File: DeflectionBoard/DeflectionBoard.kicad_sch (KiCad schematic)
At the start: 0 parts

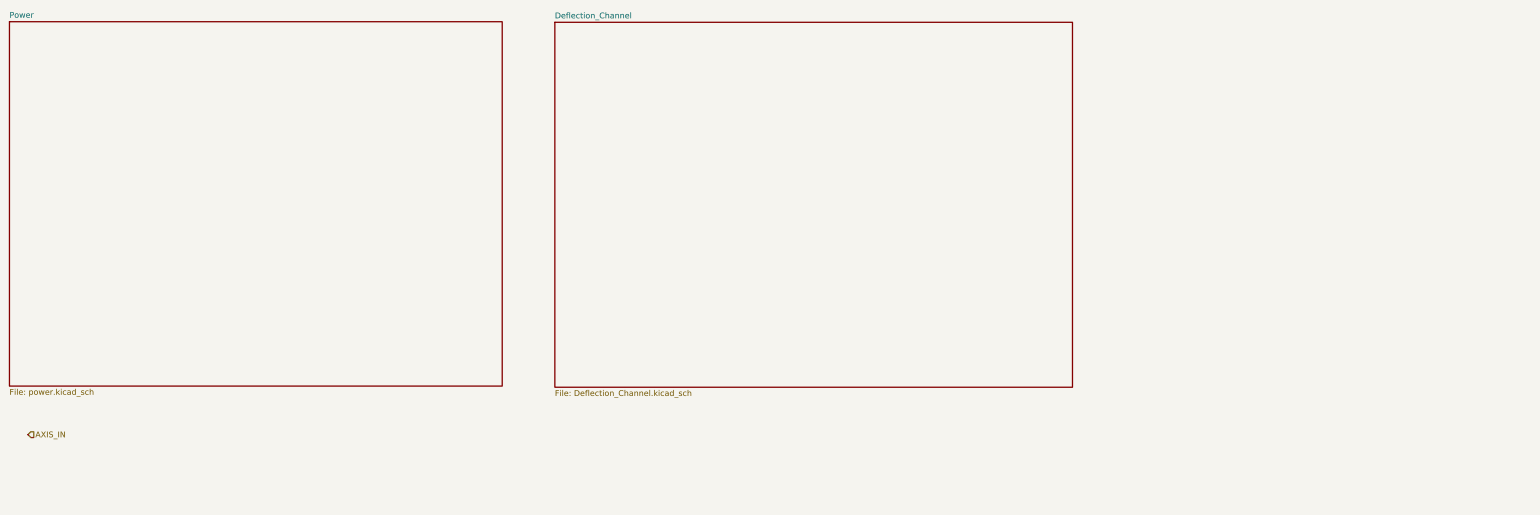
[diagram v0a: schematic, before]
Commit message: DeflectionBoard: channel X + power schematic complete, ERC clean
Full-bridge hysteretic current-mode deflection channel (CSD97394Q4M),
INA240 current sense, OPA2196 input scale, TLV3501 comparator, EN pull-up.
Power: TPS55340 boost (R106=78.7k/~600kHz), AP63205 buck 5V, REF3325 Vmid.
Hierarchical: root + Power + Deflection_Channel sheets, AXIS_IN sheet pin
wired to input connector. 0 ERC violations.

Co-Authored-By: Claude Opus 4.8 <noreply@anthropic.com>
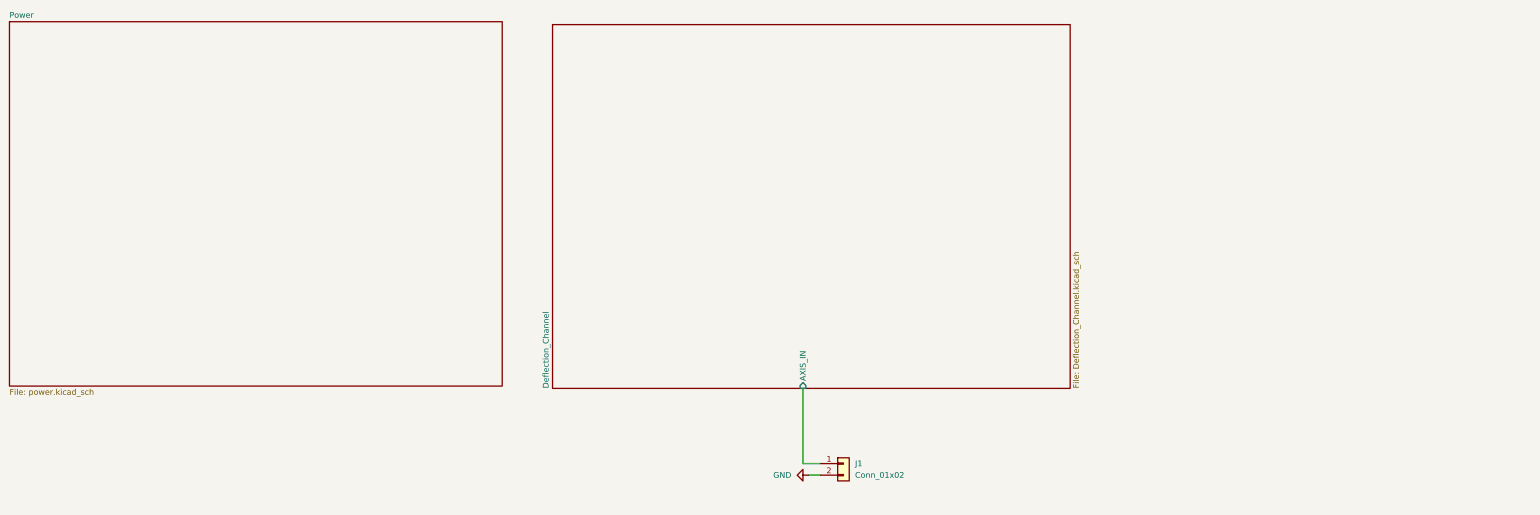
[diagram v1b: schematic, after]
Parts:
- added J1: Conn_01x02, symbol Connector_Generic:Conn_01x02
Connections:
- new net Deflection_Channel/AXIS_IN: J1.1 (Pin_1)
- new net GND: J1.2 (Pin_2)
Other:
- sheet Deflection_Channel ports: added AXIS_IN; removed none
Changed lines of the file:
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@@
 	(generator_version "10.0")
 	(paper "A3")
-	(hierarchical_label "AXIS_IN"
-		(shape input)
-		(at 30.48 115.57 0)
-		(effects
-			(font
-				(size 1.27 1.27)
-			)
-			(justify left)
+	(wire
+		(pts
+			(xy 200.66 105.41) (xy 200.66 121.92)
+		)
+		(stroke
+			(width 0)
+			(type default)
+		)
+	)
+	(wire
+		(pts
+			(xy 200.66 121.92) (xy 204.47 121.92)
+		)
+		(stroke
+			(width 0)
+			(type default)
+		)
+	)
+	(wire
+		(pts
+			(xy 201.93 124.46) (xy 204.47 124.46)
+		)
+		(stroke
+			(width 0)
+			(type default)
+		)
+	)
+	(symbol
+		(lib_id "Connector_Generic:Conn_01x02")
+		(at 209.55 121.92 0)
+		(unit 1)
+		(body_style 1)
+		(exclude_from_sim no)
+		(in_bom yes)
+		(on_board yes)
+		(in_pos_files yes)
+		(dnp no)
+		(fields_autoplaced yes)
+		(property "Reference" "J1"
+			(at 212.09 121.9199 0)
+			(show_name no)
+			(do_not_autoplace no)
+			(effects
+				(font
+					(size 1.27 1.27)
+				)
+				(justify left)
+			)
+		)
+		(property "Value" "Conn_01x02"
+			(at 212.09 124.4599 0)
+			(show_name no)
+			(do_not_autoplace no)
+			(effects
+				(font
+					(size 1.27 1.27)
+				)
+				(justify left)
+			)
+		)
+		(property "Footprint" ""
+			(at 209.55 121.92 0)
+			(hide yes)
+			(show_name no)
+			(do_not_autoplace no)
+			(effects
+				(font
+					(size 1.27 1.27)
+				)
+			)
+		)
+		(property "Datasheet" ""
+			(at 209.55 121.92 0)
+			(hide yes)
+			(show_name no)
+			(do_not_autoplace no)
+			(effects
+				(font
+					(size 1.27 1.27)
+				)
+			)
+		)
+		(property "Description" "Generic connector, single row, 01x02, script generated (kicad-library-utils/schlib/autogen/connector/)"
+			(at 209.55 121.92 0)
+			(hide yes)
+			(show_name no)
+			(do_not_autoplace no)
+			(effects
+				(font
+					(size 1.27 1.27)
+				)
+			)
+		)
+		(pin "1"
+		)
+		(pin "2"
+		)
+		(instances
+			(project "DeflectionBoard"
+				(path "/6f717d52-0a9b-43ca-aa24-dc6f278930de"
+					(reference "J1")
+					(unit 1)
+				)
+			)
+		)
+	)
+	(symbol
+		(lib_id "power:GND")
+		(at 201.93 124.46 270)
+		(unit 1)
+		(body_style 1)
+		(exclude_from_sim no)
+		(in_bom yes)
+		(on_board yes)
+		(in_pos_files yes)
+		(dnp no)
+		(fields_autoplaced yes)
+		(property "Reference" "#PWR01"
+			(at 195.58 124.46 0)
+			(hide yes)
+			(show_name no)
+			(do_not_autoplace no)
+			(effects
+				(font
+					(size 1.27 1.27)
+				)
+			)
+		)
+		(property "Value" "GND"
+			(at 198.12 124.4599 90)
+			(show_name no)
+			(do_not_autoplace no)
+			(effects
+				(font
+					(size 1.27 1.27)
+				)
+				(justify right)
+			)
+		)
+		(property "Footprint" ""
+			(at 201.93 124.46 0)
+			(hide yes)
+			(show_name no)
+			(do_not_autoplace no)
+			(effects
+				(font
+					(size 1.27 1.27)
+				)
+			)
+		)
+		(property "Datasheet" ""
+			(at 201.93 124.46 0)
+			(hide yes)
+			(show_name no)
+			(do_not_autoplace no)
+			(effects
+				(font
+					(size 1.27 1.27)
+				)
+			)
+		)
+		(property "Description" "Power symbol creates a global label with name \"GND\" , ground"
+			(at 201.93 124.46 0)
+			(hide yes)
+			(show_name no)
+			(do_not_autoplace no)
+			(effects
+				(font
+					(size 1.27 1.27)
+				)
+			)
+		)
+		(pin "1"
+		)
+		(instances
+			(project "DeflectionBoard"
+				(path "/6f717d52-0a9b-43ca-aa24-dc6f278930de"
+					(reference "#PWR01")
+					(unit 1)
+				)
+			)
 		)
 	)
 	(sheet
-		(at 146.177 25.019)
-		(size 113.665 80.137)
+		(at 145.669 25.527)
+		(size 113.665 79.883)
 		(exclude_from_sim no)
 		(in_bom yes)
@@
 		)
 		(property "Sheetname" "Deflection_Channel"
-			(at 146.177 24.3074 0)
+			(at 144.9574 105.41 90)
 			(show_name no)
 			(do_not_autoplace no)
@@
 		)
 		(property "Sheetfile" "Deflection_Channel.kicad_sch"
-			(at 146.177 105.7406 0)
+			(at 259.9186 105.41 90)
 			(show_name no)
 			(do_not_autoplace no)
@@
 			)
 		)
+		(pin "AXIS_IN" input
+			(at 200.66 105.41 270)
+			(effects
+				(font
+					(size 1.27 1.27)
+				)
+				(justify left)
+			)
+		)

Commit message: DeflectionBoard: channel Y instanced, footprints assigned, ERC clean
- Y axis = 2nd instance of Deflection_Channel sheet (X=2xx, Y=3xx)
- Signal labels made local (per-instance scoping), power refs uniquified
- Footprints: 0402 passives, R201/R301 shunt=2512, D102=SS54/SMB,
  J1=PH 4p / J101=VH power / yoke=XH (keyed), L101=12x12 / L102=SRN6045
- E96 1% feedback/timing resistors (137k/53.6k/78.7k)

Co-Authored-By: Claude Opus 4.8 <noreply@anthropic.com>
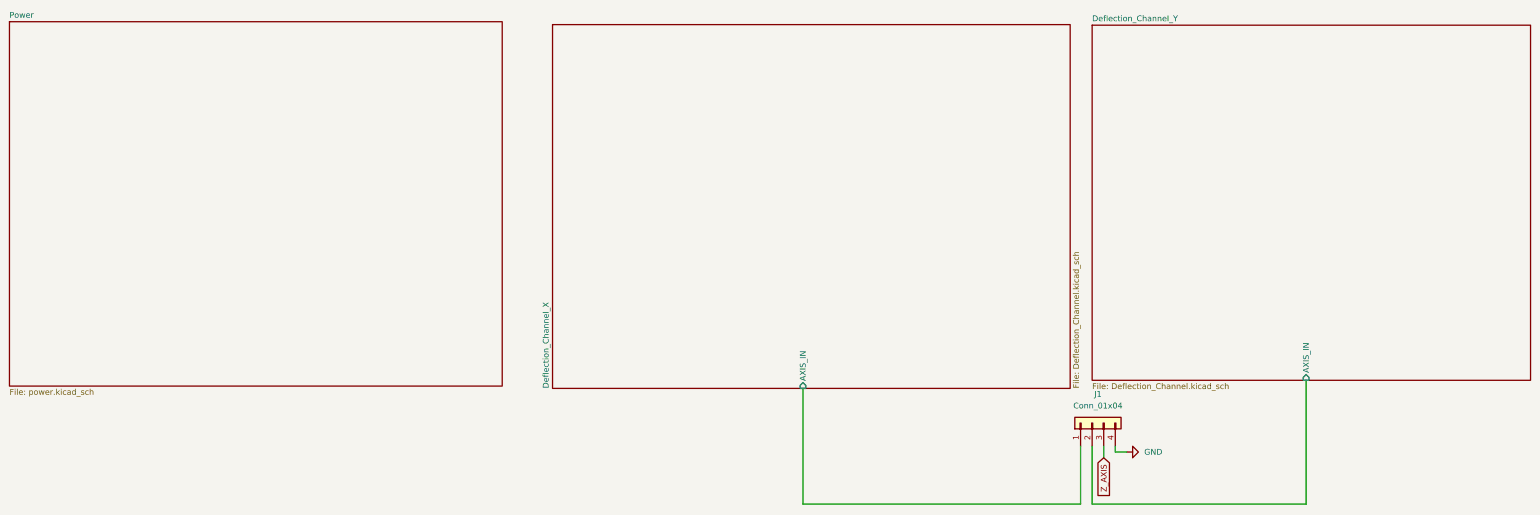
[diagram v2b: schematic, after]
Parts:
- removed J1: Conn_01x02, symbol Connector_Generic:Conn_01x02
- added J1: Conn_01x04, Connector_JST:JST_PH_B4B-PH-K_1x04_P2.00mm_Vertical, symbol Connector_Generic:Conn_01x04
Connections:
- net Deflection_Channel_X/AXIS_IN: now also J1.1 (Pin_1)
- net GND: now also J1.4 (Pin_4)
- new net Deflection_Channel_Y/AXIS_IN: J1.2 (Pin_2)
- new net Z_AXIS: J1.3 (Pin_3)
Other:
- sheet Deflection_Channel renamed Deflection_Channel_X
- added sheet Deflection_Channel_Y (Deflection_Channel.kicad_sch)
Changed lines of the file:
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@@
 	(wire
 		(pts
-			(xy 200.66 105.41) (xy 200.66 121.92)
-		)
-		(stroke
-			(width 0)
-			(type default)
-		)
-	)
-	(wire
-		(pts
-			(xy 200.66 121.92) (xy 204.47 121.92)
-		)
-		(stroke
-			(width 0)
-			(type default)
-		)
-	)
-	(wire
-		(pts
-			(xy 201.93 124.46) (xy 204.47 124.46)
-		)
-		(stroke
-			(width 0)
-			(type default)
+			(xy 266.7 118.11) (xy 266.7 120.65)
+		)
+		(stroke
+			(width 0)
+			(type default)
+		)
+	)
+	(wire
+		(pts
+			(xy 269.24 119.38) (xy 271.78 119.38)
+		)
+		(stroke
+			(width 0)
+			(type default)
+		)
+	)
+	(wire
+		(pts
+			(xy 261.62 130.81) (xy 261.62 118.11)
+		)
+		(stroke
+			(width 0)
+			(type default)
+		)
+	)
+	(wire
+		(pts
+			(xy 311.15 103.632) (xy 311.15 130.81)
+		)
+		(stroke
+			(width 0)
+			(type default)
+		)
+	)
+	(wire
+		(pts
+			(xy 200.66 105.41) (xy 200.66 130.81)
+		)
+		(stroke
+			(width 0)
+			(type default)
+		)
+	)
+	(wire
+		(pts
+			(xy 264.16 130.81) (xy 311.15 130.81)
+		)
+		(stroke
+			(width 0)
+			(type default)
+		)
+	)
+	(wire
+		(pts
+			(xy 264.16 118.11) (xy 264.16 130.81)
+		)
+		(stroke
+			(width 0)
+			(type default)
+		)
+	)
+	(wire
+		(pts
+			(xy 200.66 130.81) (xy 261.62 130.81)
+		)
+		(stroke
+			(width 0)
+			(type default)
+		)
+	)
+	(wire
+		(pts
+			(xy 269.24 118.11) (xy 269.24 119.38)
+		)
+		(stroke
+			(width 0)
+			(type default)
+		)
+	)
+	(global_label "Z_AXIS"
+		(shape input)
+		(at 266.7 120.65 270)
+		(fields_autoplaced yes)
+		(effects
+			(font
+				(size 1.27 1.27)
+			)
+			(justify right)
+		)
+		(property "Intersheetrefs" "${INTERSHEET_REFS}"
+			(at 266.7 129.9247 90)
+			(hide yes)
+			(show_name no)
+			(do_not_autoplace no)
+			(effects
+				(font
+					(size 1.27 1.27)
+				)
+				(justify right)
+			)
 		)
 	)
 	(symbol
-		(lib_id "Connector_Generic:Conn_01x02")
-		(at 209.55 121.92 0)
+		(lib_id "Connector_Generic:Conn_01x04")
+		(at 264.16 113.03 90)
 		(unit 1)
 		(body_style 1)
@@
 		(fields_autoplaced yes)
 		(property "Reference" "J1"
-			(at 212.09 121.9199 0)
-			(show_name no)
-			(do_not_autoplace no)
-			(effects
-				(font
-					(size 1.27 1.27)
-				)
-				(justify left)
-			)
-		)
-		(property "Value" "Conn_01x02"
-			(at 212.09 124.4599 0)
-			(show_name no)
-			(do_not_autoplace no)
-			(effects
-				(font
-					(size 1.27 1.27)
-				)
-				(justify left)
-			)
-		)
-		(property "Footprint" ""
-			(at 209.55 121.92 0)
+			(at 265.43 106.68 90)
+			(show_name no)
+			(do_not_autoplace no)
+			(effects
+				(font
+					(size 1.27 1.27)
+				)
+			)
+		)
+		(property "Value" "Conn_01x04"
+			(at 265.43 109.22 90)
+			(show_name no)
+			(do_not_autoplace no)
+			(effects
+				(font
+					(size 1.27 1.27)
+				)
+			)
+		)
+		(property "Footprint" "Connector_JST:JST_PH_B4B-PH-K_1x04_P2.00mm_Vertical"
+			(at 264.16 113.03 0)
 			(hide yes)
 			(show_name no)
@@
 		)
 		(property "Datasheet" ""
-			(at 209.55 121.92 0)
-			(hide yes)
-			(show_name no)
-			(do_not_autoplace no)
-			(effects
-				(font
-					(size 1.27 1.27)
-				)
-			)
-		)
-		(property "Description" "Generic connector, single row, 01x02, script generated (kicad-library-utils/schlib/autogen/connector/)"
-			(at 209.55 121.92 0)
+			(at 264.16 113.03 0)
+			(hide yes)
+			(show_name no)
+			(do_not_autoplace no)
+			(effects
+				(font
+					(size 1.27 1.27)
+				)
+			)
+		)
+		(property "Description" "Generic connector, single row, 01x04, script generated (kicad-library-utils/schlib/autogen/connector/)"
+			(at 264.16 113.03 0)
 			(hide yes)
 			(show_name no)
@@
 		)
 		(pin "1"
+		)
+		(pin "4"
+		)
+		(pin "3"
 		)
 		(pin "2"
@@
 	(symbol
 		(lib_id "power:GND")
-		(at 201.93 124.46 270)
+		(at 271.78 119.38 90)
 		(unit 1)
 		(body_style 1)
@@
 		(dnp no)
 		(fields_autoplaced yes)
-		(property "Reference" "#PWR01"
-			(at 195.58 124.46 0)
+		(property "Reference" "#PWR0301"
+			(at 278.13 119.38 0)
 			(hide yes)
 			(show_name no)
@@
 		)
 		(property "Value" "GND"
-			(at 198.12 124.4599 90)
+			(at 275.59 119.3799 90)
 			(show_name no)
 			(do_not_autoplace no)
@@
 		)
 		(property "Footprint" ""
-			(at 201.93 124.46 0)
+			(at 271.78 119.38 0)
 			(hide yes)
 			(show_name no)
@@
 		)
 		(property "Datasheet" ""
-			(at 201.93 124.46 0)
+			(at 271.78 119.38 0)
 			(hide yes)
 			(show_name no)
@@
 		)
 		(property "Description" "Power symbol creates a global label with name \"GND\" , ground"
-			(at 201.93 124.46 0)
+			(at 271.78 119.38 0)
 			(hide yes)
 			(show_name no)
@@
 			(project "DeflectionBoard"
 				(path "/6f717d52-0a9b-43ca-aa24-dc6f278930de"
-					(reference "#PWR01")
+					(reference "#PWR0301")
 					(unit 1)
 				)
@@
 			(color 0 0 0 0)
 		)
-		(property "Sheetname" "Deflection_Channel"
+		(property "Sheetname" "Deflection_Channel_X"
 			(at 144.9574 105.41 90)
 			(show_name no)
@@
 				)
 			)
+		)
+	)
+	(sheet
+		(at 264.16 25.654)
+		(size 96.266 77.978)
+		(exclude_from_sim no)
+		(in_bom yes)
+		(on_board yes)
+		(dnp no)
+		(fields_autoplaced yes)
+		(stroke
+			(width 0.1524)
+			(type solid)
+		)
+		(fill
+			(color 0 0 0 0)
+		)
+		(property "Sheetname" "Deflection_Channel_Y"
+			(at 264.16 24.9424 0)
+			(show_name no)
+			(do_not_autoplace no)
+			(effects
+				(font
+					(size 1.27 1.27)
+				)
+				(justify left bottom)
+			)
+		)
+		(property "Sheetfile" "Deflection_Channel.kicad_sch"
+			(at 264.16 104.2166 0)
+			(show_name no)
+			(do_not_autoplace no)
+			(effects
+				(font
+					(size 1.27 1.27)
+				)
+				(justify left top)
+			)
+		)
+		(pin "AXIS_IN" input
+			(at 311.15 103.632 270)
+			(effects
+				(font
+					(size 1.27 1.27)
+				)
+				(justify left)
+			)
+		)
+		(instances
+			(project "DeflectionBoard"
+				(path "/6f717d52-0a9b-43ca-aa24-dc6f278930de"
+					(page "4")
+				)
+			)

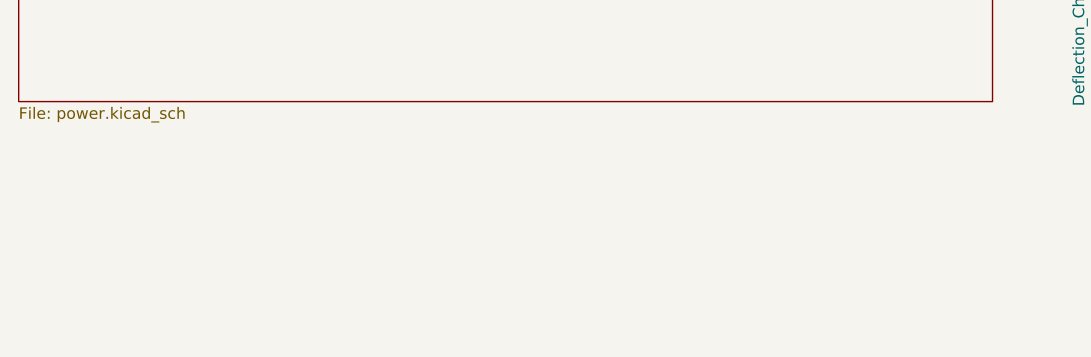
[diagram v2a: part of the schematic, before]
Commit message: DeflectionBoard: full PCB routing complete, DRC clean
- Channel X + Y fully routed (0 unconnected), power section + GND pour
- Power netclasses: +7.5V/+15V wide (1.8mm), +5V/yoke/SW (1.0mm), signals 0.25mm
- Manual neck-down to fine-pitch power pins; thermal/stitching vias
- Only 5 benign lib_footprint_mismatch warnings remain (no fab impact)

Co-Authored-By: Claude Opus 4.8 <noreply@anthropic.com>
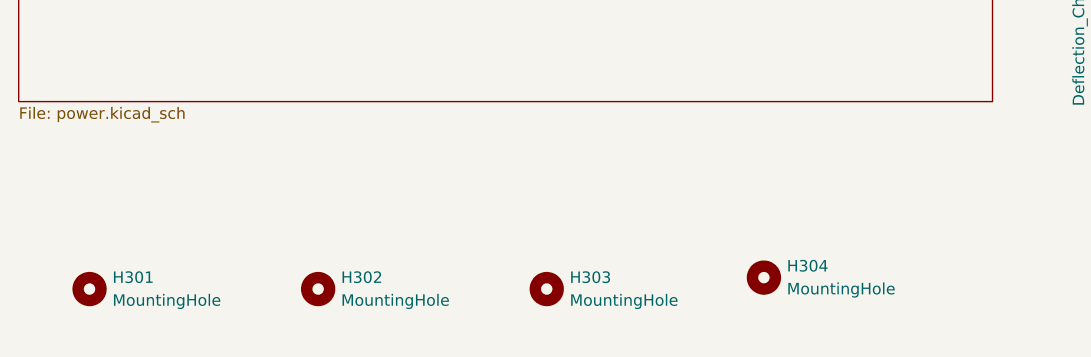
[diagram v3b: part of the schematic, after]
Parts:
- added H301, H302, H303, H304: MountingHole, symbol Mechanical:MountingHole
